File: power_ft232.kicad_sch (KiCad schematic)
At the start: 5 parts

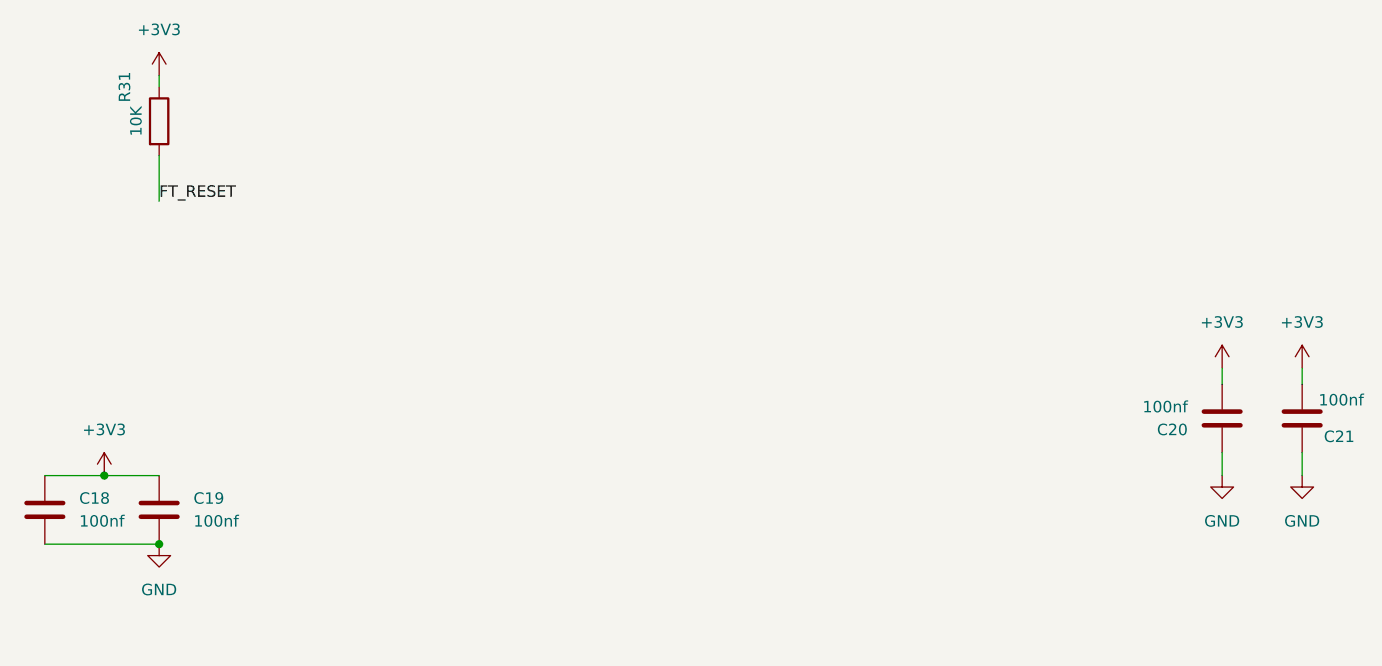
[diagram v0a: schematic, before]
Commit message: feat: PCB layout updates, schematic changes, fp-lib-table config
- cnc_pic32.kicad_pcb: component repositioning, board outline, text formatting
- cnc_pic32.kicad_prl/pro: project settings updates
- fp-lib-table: add Library path to Library.pretty
- mcu.kicad_sch: PIC32 pin configuration updates
- zigbee.kicad_sch: MRF24J40 module updates
- oscilator.kicad_sch: crystal configuration
- power.kicad_sch/power_ft232.kicad_sch: power supply updates
- oled.kicad_sch: OLED display connections
- idc.kicad_sch: IDC connector updates
- osc_ft232.kicad_sch: FT232 crystal
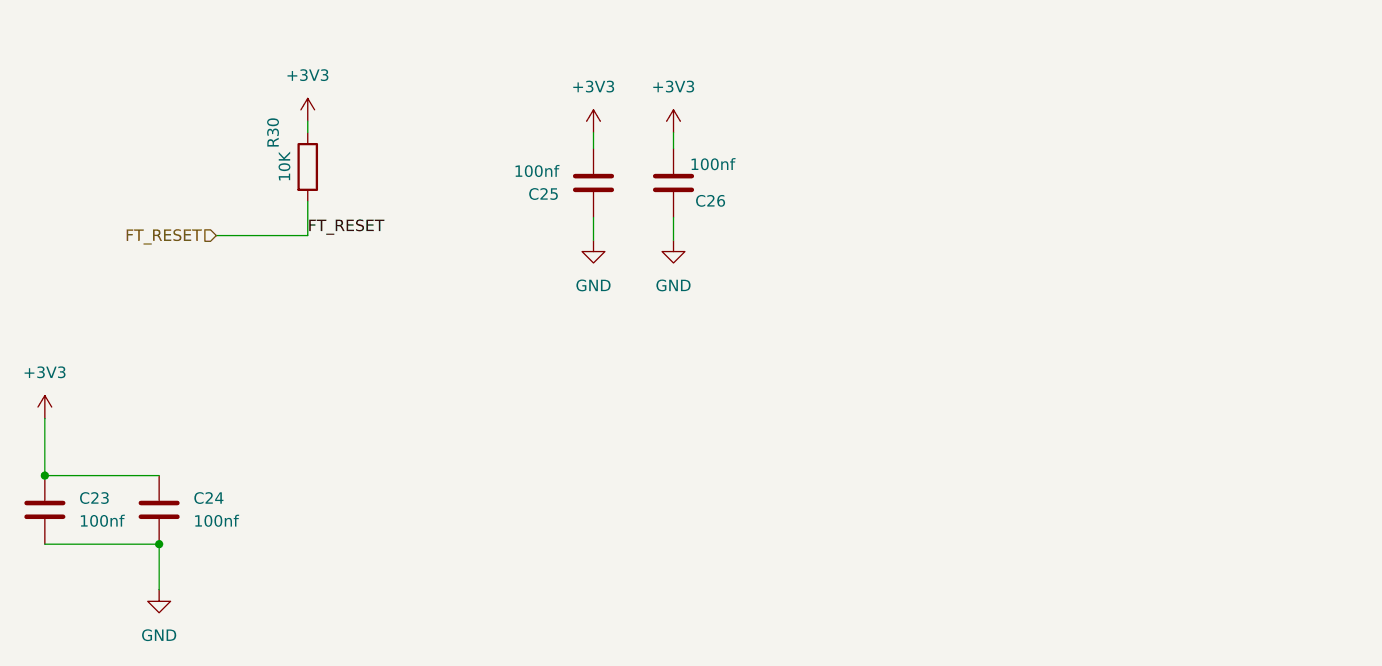
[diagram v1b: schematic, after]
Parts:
- renumbered C18 to C23, C19 to C24, C20 to C25, C21 to C26, R31 to R30
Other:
- moved on the sheet: C25, C26, R30
